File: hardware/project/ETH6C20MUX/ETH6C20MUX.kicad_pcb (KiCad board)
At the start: 4 copper layers, 160 x 100 mm, 184 parts, among them J301 5499141-4, J501 Conn_01x06, J502 Conn_02x08_Odd_Even, J503 C64AC, J601 Conn_02x05, J602 Conn_02x01, K301 HE3621A0510, K302 HE3621A0510, K303 HE3621A0510, K304 HE3621A0510, K305 HE3621A0510, K306 HE3621A0510, K307 HE3621A0510, K308 HE3621A0510, K309 HE3621A0510, K310 HE3621A0510, K311 HE3621A0510, K312 HE3621A0510, K313 HE3621A0510, K314 HE3621A0510, K315 HE3621A0510, K316 HE3621A0510, K317 HE3621A0510, K318 HE3621A0510, K319 HE3621A0510, K320 HE3621A0510, K321 HE3621A0510, K322 HE3621A0510, K323 HE3621A0510, K324 HE3621A0510, K325 HE3621A0510, K326 HE3621A0510, K327 HE3621A0510, K328 HE3621A0510, K329 HE3621A0510, K330 HE3621A0510, K331 HE3621A0510, K332 HE3621A0510, K333 HE3621A0510, K334 HE3621A0510, K335 HE3621A0510, K336 HE3621A0510, K337 HE3621A0510, K338 HE3621A0510, K339 HE3621A0510, K340 HE3621A0510, K341 HE3621A0510, K342 HE3621A0510, K343 HE3621A0510, K344 HE3621A0510, K345 HE3621A0510, K346 HE3621A0510, K347 HE3621A0510, K348 HE3621A0510, K349 HE3621A0510, K350 HE3621A0510, K351 HE3621A0510, K352 HE3621A0510, K353 HE3621A0510, K354 HE3621A0510, K355 HE3621A0510, K356 HE3621A0510, K357 HE3621A0510, K358 HE3621A0510, K359 HE3621A0510, K360 HE3621A0510, K361 HE3621A0510, K362 HE3621A0510, K363 HE3621A0510, K364 HE3621A0510, K365 HE3621A0510, K366 HE3621A0510, Q401 IRFR5410, U201 LC03-3.3, U202 LAN8742A, U203 LC03-3.3, U301 MCZ33996, U302 MCZ33996, U303 MCZ33996, U304 MCZ33996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

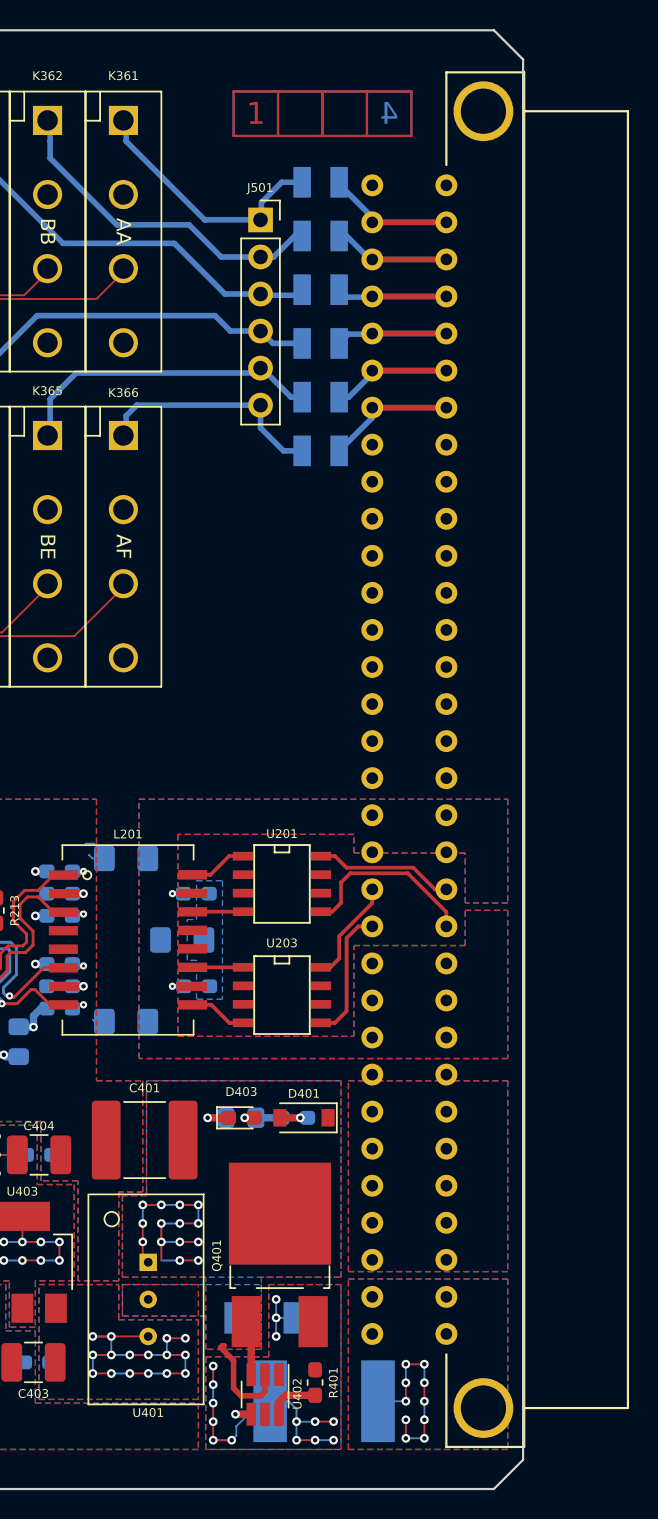
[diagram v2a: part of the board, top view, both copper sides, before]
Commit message: Added firmware software, based on zephyr OS.
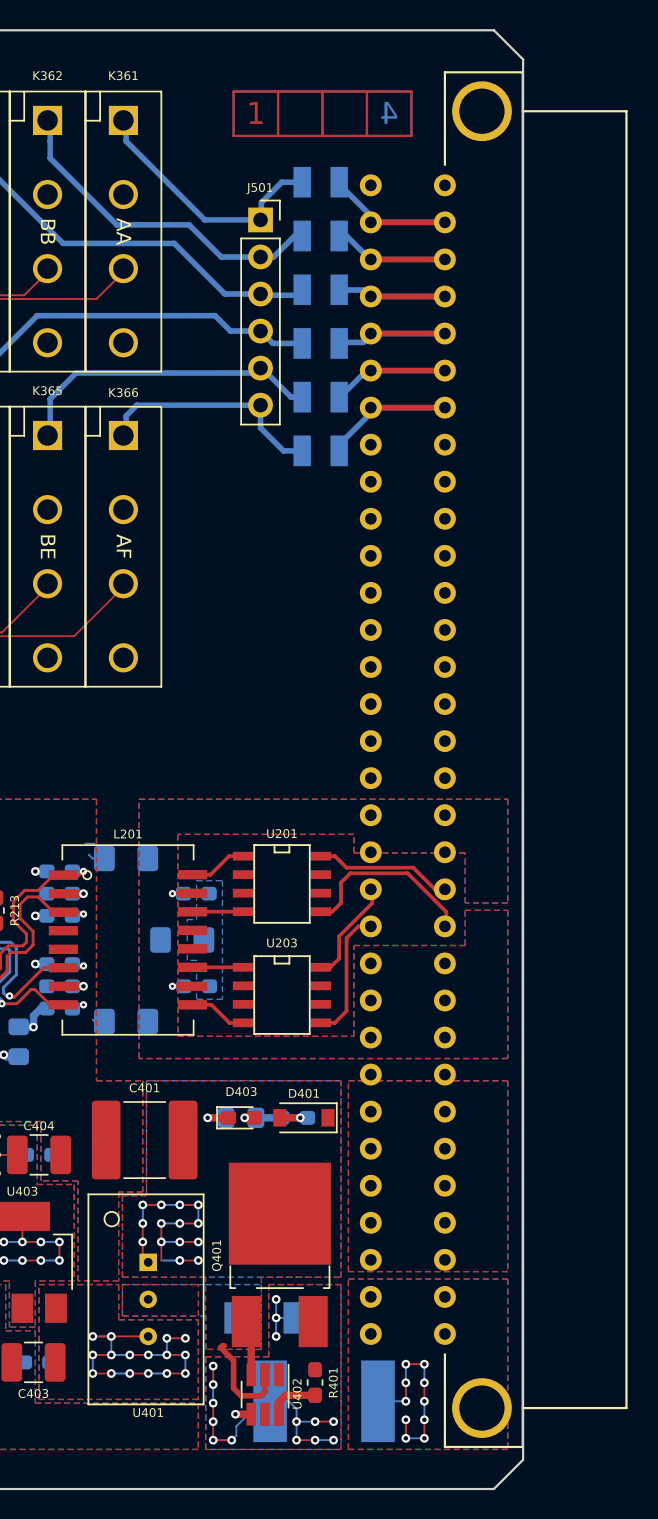
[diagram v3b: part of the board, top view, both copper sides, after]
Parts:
- moved J503 0.10 mm to (212.1, 90.0)
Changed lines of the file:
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@@
     (thickness 1.6)
     (drawings 243)
-    (tracks 3492)
+    (tracks 3493)
     (zones 0)
     (modules 184)
@@
   (page A4)
   (layers
-    (0 Top signal)
+    (0 Top signal hide)
     (1 GND power)
-    (2 Power power)
-    (31 Bottom signal)
+    (2 Power power hide)
+    (31 Bottom signal hide)
     (32 B.Adhes user)
     (33 F.Adhes user hide)
@@
     (mod_text_size 1 1)
     (mod_text_width 0.15)
-    (pad_size 5 6)
-    (pad_drill 0)
+    (pad_size 4.1 4.1)
+    (pad_drill 3.1)
     (pad_to_mask_clearance 0)
     (aux_axis_origin 0 0)
@@
     (add_net "Net-(D402-Pad1)")
     (add_net "Net-(D403-Pad2)")
-    (add_net "Net-(F501-Pad1)")
-    (add_net "Net-(F502-Pad1)")
-    (add_net "Net-(F503-Pad1)")
-    (add_net "Net-(F504-Pad1)")
-    (add_net "Net-(F505-Pad1)")
-    (add_net "Net-(F506-Pad1)")
     (add_net "Net-(L201-Pad10)")
     (add_net "Net-(L201-Pad11)")
@@
     (add_net /Relays/PIN8)
     (add_net /Relays/PIN9)
+    (add_net "Net-(F501-Pad1)")
+    (add_net "Net-(F502-Pad1)")
+    (add_net "Net-(F503-Pad1)")
+    (add_net "Net-(F504-Pad1)")
+    (add_net "Net-(F505-Pad1)")
+    (add_net "Net-(F506-Pad1)")
   )
   (module ETH6C20MUX:TSR2 (layer Top)
@@
     (fp_line (start -7.3 -3.9) (end 7.3 -3.9) (layer F.CrtYd) (width 0.12))
     (fp_line (start -7.2 -3.8) (end 7.2 -3.8) (layer F.SilkS) (width 0.12))
-    (fp_line (start -7.2 4) (end -7.2 -3.8) (layer F.SilkS) (width 0.12))
+    (fp_line (start -7.2 4.1) (end -7.2 -3.8) (layer F.SilkS) (width 0.12))
     (fp_line (start 7.2 4.1) (end -7.2 4.1) (layer F.SilkS) (width 0.12))
     (fp_line (start 7.2 -3.8) (end 7.2 4.1) (layer F.SilkS) (width 0.12))
@@
       (net 7 "Net-(C401-Pad1)"))
     (model ${ETH6C20MUX}/tsr2.STEP
-      (offset (xyz 0 0.15 10.05))
+      (offset (xyz 0 -0.15 10.05))
       (scale (xyz 1 1 1))
-      (rotate (xyz 180 0 0))
+      (rotate (xyz 180 0 180))
     )
   )
@@
   )
   (module ETH6C20MUX:Socket_DIN41612-CaseC1-AC-Male-64Pin-2rows (layer Top)
-    (at 212.2 90 90)
+    (at 212.1 90 90)
     (fp_text reference J503 (at 46.622 1.859 90) (layer F.SilkS) hide
       (effects (font (size 0.6 0.6) (thickness 0.12)))
@@
       (net 58 +24V))
     (pad 1 thru_hole circle (at -44.45 5.08 90) (size 4.1 4.1) (drill 3.1) (layers *.Cu *.Mask)
-      (clearance 1))
+      (clearance 1.27))
     (pad 1 thru_hole circle (at 44.45 5.08 90) (size 4.1 4.1) (drill 3.1) (layers *.Cu *.Mask)
-      (clearance 1))
+      (clearance 1.27))
     (model ${ETH6C20MUX}/DIN41612_64ac_male_ra.wrl
       (offset (xyz 0 -15.31619976997376 3.936999940872192))
@@
     )
     (pad 1 thru_hole circle (at 0 0) (size 5.6 5.6) (drill 3.2) (layers *.Cu *.Mask)
-      (clearance 0.508))
+      (clearance 0.753))
   )
   (module MountingHole:MountingHole_3.2mm_M3_DIN965_Pad (layer Top)
@@
     )
     (pad 1 thru_hole circle (at 0 0) (size 5.6 5.6) (drill 3.2) (layers *.Cu *.Mask)
-      (clearance 0.508))
+      (clearance 0.753))
   )
   (module Package_TO_SOT_SMD:SOT-23-6_Handsoldering (layer Top)
@@
   (segment (start 209.76 58.25) (end 213.778534 58.25) (width 0.381) (layer Top) (net 134))
   (segment (start 209.66 58.25) (end 214.74 58.25) (width 0.381) (layer Bottom) (net 134))
-  (segment (start 209.617 58.293) (end 209.66 58.25) (width 0.381) (layer Bottom) (net 134))
-  (segment (start 207.391 57.785) (end 207.899 58.293) (width 0.381) (layer Bottom) (net 134))
-  (segment (start 207.899 58.293) (end 209.617 58.293) (width 0.381) (layer Bottom) (net 134))
+  (segment (start 209.21 57.8) (end 209.66 58.25) (width 0.381) (layer Bottom) (net 134))
+  (segment (start 207.391 57.785) (end 207.406 57.8) (width 0.381) (layer Bottom) (net 134))
+  (segment (start 207.406 57.8) (end 209.21 57.8) (width 0.381) (layer Bottom) (net 134))
   (segment (start 209.76 60.79) (end 214.84 60.79) (width 0.381) (layer Top) (net 135))
   (segment (start 209.66 60.79) (end 214.74 60.79) (width 0.381) (layer Bottom) (net 135))
-  (segment (start 209.617 60.833) (end 209.66 60.79) (width 0.381) (layer Bottom) (net 135))
-  (segment (start 207.391 61.468) (end 208.026 60.833) (width 0.381) (layer Bottom) (net 135))
-  (segment (start 208.026 60.833) (end 209.617 60.833) (width 0.381) (layer Bottom) (net 135))
+  (segment (start 209.05 61.4) (end 209.66 60.79) (width 0.381) (layer Bottom) (net 135))
+  (segment (start 207.391 61.468) (end 207.459 61.4) (width 0.381) (layer Bottom) (net 135))
+  (segment (start 207.459 61.4) (end 209.05 61.4) (width 0.381) (layer Bottom) (net 135))
   (segment (start 209.76 63.33) (end 214.84 63.33) (width 0.381) (layer Top) (net 136))
   (segment (start 209.66 63.33) (end 214.74 63.33) (width 0.381) (layer Bottom) (net 136))
-  (segment (start 209.66 63.54) (end 209.66 63.33) (width 0.381) (layer Bottom) (net 136))
-  (segment (start 207.391 65.151) (end 208.049 65.151) (width 0.381) (layer Bottom) (net 136))
-  (segment (start 208.049 65.151) (end 209.66 63.54) (width 0.381) (layer Bottom) (net 136))
+  (segment (start 209.27 63.33) (end 209.66 63.33) (width 0.381) (layer Bottom) (net 136))
+  (segment (start 207.391 65.151) (end 207.449 65.151) (width 0.381) (layer Bottom) (net 136))
+  (segment (start 207.449 65.151) (end 209.27 63.33) (width 0.381) (layer Bottom) (net 136))
   (segment (start 209.76 65.87) (end 214.84 65.87) (width 0.381) (layer Top) (net 137))
   (segment (start 209.66 65.87) (end 214.74 65.87) (width 0.381) (layer Bottom) (net 137))
-  (segment (start 209.66 66.565) (end 209.66 65.87) (width 0.381) (layer Bottom) (net 137))
-  (segment (start 207.391 68.834) (end 209.66 66.565) (width 0.381) (layer Bottom) (net 137))
+  (segment (start 209.66 66.14) (end 209.66 65.87) (width 0.381) (layer Bottom) (net 137))
+  (segment (start 207.391 68.834) (end 207.391 68.409) (width 0.381) (layer Bottom) (net 137))
+  (segment (start 207.391 68.409) (end 209.66 66.14) (width 0.381) (layer Bottom) (net 137))
   (via (at 186.436 108.331) (size 0.6) (drill 0.3) (layers Top Bottom) (net 138))
   (via (at 182.245 106.299) (size 0.6) (drill 0.3) (layers Top Bottom) (net 138))
@@
   )
   (zone (net 4) (net_name Earth) (layer Top) (hatch edge 0.508)
-    (connect_pads (clearance 0.127))
+    (connect_pads (clearance 0.508))
     (min_thickness 0.12)
     (fill yes (arc_segments 32) (thermal_gap 0.127) (thermal_bridge_width 0.508) (smoothing chamfer) (radius 0.254))
@@
   )
   (zone (net 4) (net_name Earth) (layer GND) (hatch edge 0.508)
-    (connect_pads yes (clearance 0.127))
+    (connect_pads yes (clearance 0.254))
     (min_thickness 0.12)
     (fill yes (arc_segments 32) (thermal_gap 0.127) (thermal_bridge_width 0.508) (smoothing chamfer) (radius 0.254))
@@
   )
   (zone (net 4) (net_name Earth) (layer Bottom) (hatch edge 0.508)
-    (connect_pads (clearance 0.127))
+    (connect_pads (clearance 0.508))
     (min_thickness 0.12)
     (fill yes (arc_segments 32) (thermal_gap 0.127) (thermal_bridge_width 0.508) (smoothing chamfer) (radius 0.254))

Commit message: Small updates in PCB design.
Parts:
- K301, K302, K303, K304, K305, K306, K307, K308, K309, K310, K311, K312, K313, K314, K315, K316, K317, K318, K319, K320, K321, K322, K323, K324, K325, K326, K327, K328, K329, K330, K331, K332, K333, K334, K335, K336, K337, K338, K339, K340, K341, K342, K343, K344, K345, K346, K347, K348, K349, K350, K351, K352, K353, K354, K355, K356, K357, K358, K359, K360, K361, K362, K363, K364, K365, K366: footprint ETH6C20MUX:HE360_x-5331272-5 -> ETH6C20MUX:HE360_x-5050462-8
